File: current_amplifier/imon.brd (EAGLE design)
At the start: 76 x 16 mm, 73 parts, among them U2 OPAMP_DUALFAN4852, U4 AD8418, U5 MCP1501", U6 LTC2312-12

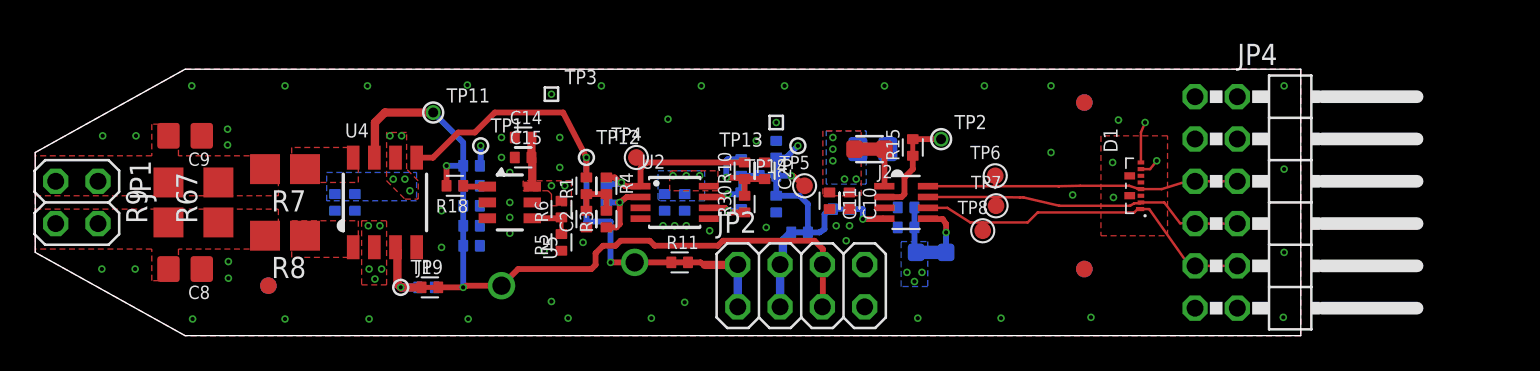
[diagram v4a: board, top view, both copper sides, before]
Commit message: imon board passes 6mil DRC.  The gain on the 4th order Bessel filter is probably wrong and needs to be redone, but the layout is ready for review
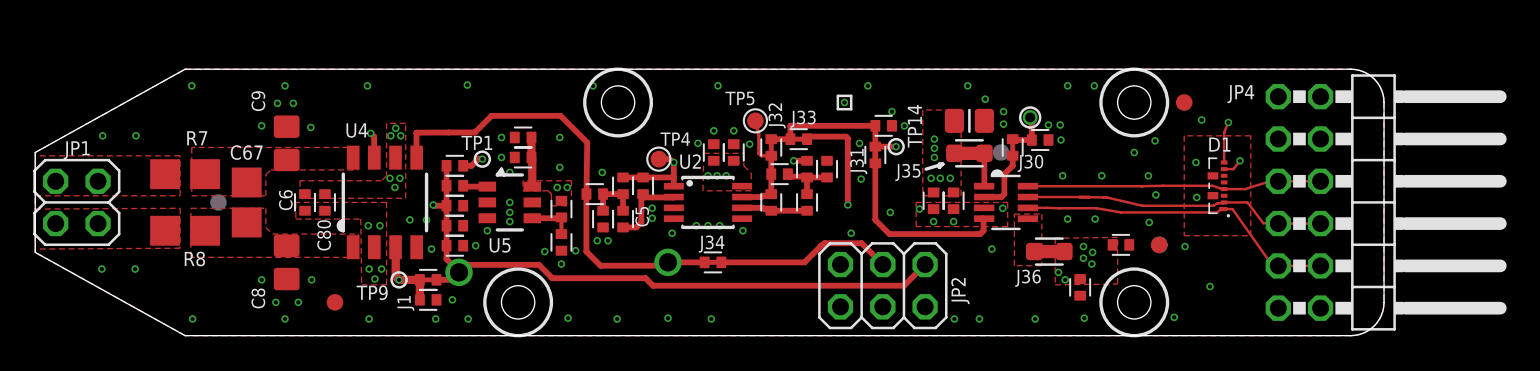
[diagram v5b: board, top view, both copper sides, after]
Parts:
- removed J2, J3: (no value), marionette:JUMPER-SHORTED-CUTTABLE-E0603-0.8MM
- removed R11, R15, R16, R17, R2: (no value), marionette:JUMPER-SHORTED-CUTTABLE-E0402-0.3MM
- removed R13, R14: np, rcl_custom:.0402-B
- removed R67, R9: np, rcl_custom:1206-0402
- removed TP11: PAD+VIA_0.6MM, marionette:PAD+VIA_0.6MM
- removed TP12: PAD+VIA_0.25MM, marionette:PAD+VIA_0.25MM
- removed TP3: PAD+VIA_GND_0.25MM, marionette:PAD+GND_VIA_0.25MM
- removed TP6, TP7, TP8: (no value), marionette:PAD-ROUND-1.0-NOCREAM+SILK
- added C16: np, rcl_custom:.0402-B
- added C67: np, rcl_custom:1206-0402
- added H1, H2, H3, H4: M2-BARE_MOUNTING_HOLE, marionette:M2-BARE_MOUNTING_HOLE
- added J30, J31, J32, J33, J34: (no value), marionette:JUMPER-SHORTED-CUTTABLE-E0402-0.3MM
- added J35, J36: (no value), marionette:JUMPER-SHORTED-CUTTABLE-E0603-0.8MM
- JP2: device pinhead:2X04 -> pinhead:2X03
- moved C12 13.1 mm to (65.2, 5.45), flipped to the top
- moved C19 11.1 mm to (62.8, 2.90), flipped to the top, turned to 270 degrees
- moved C18 6.60 mm to (51.0, 12.6), flipped to the top, turned to 180 degrees
- moved C10 6.25 mm to (55.1, 8.10)
- moved C11 6.25 mm to (54.0, 8.10)
- moved C9 6.12 mm to (15.1, 11.6), turned to 270 degrees
- moved C8 6.11 mm to (15.1, 4.40), turned to 90 degrees
- moved C13 6.04 mm to (56.1, 12.9), flipped to the top, turned to 0 degrees
- moved R7 6.01 mm to (9.00, 9.70)
- moved R8 6.01 mm to (9.00, 6.30)
- moved FIDUCIAL4 6.00 mm to (69.0, 14.0)
- moved U6 6.00 mm to (58.3, 8.00)
- moved TP14 5.90 mm to (51.7, 11.3)
- moved FIDUCIAL1 5.83 mm to (58.0, 11.0)
- moved FIDUCIAL3 5.83 mm to (11.0, 8.00)
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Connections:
- removed net V3.3D: C12.1, C19.1, D1.7, J3.2, JP4.3, JP4.4
- removed net V5D: C10.1, C11.1, C13.1, C14.2, C15.2, C3.1, C4.1, C6.1, C80.1, D1.8, J2.2, JP4.1, JP4.2, R6.2, U2.8, U4.6, U5.6
- new net VDD: C10.1, C11.1, C13.1, C14.2, C15.2, C3.1, C4.1, C6.1, C80.1, D1.8, J35.2, JP4.1, JP4.2, R6.2, U2.8, U4.6, U5.6
- new net VIO: C12.1, C19.1, D1.7, J36.2, JP4.3, JP4.4
- net ADC_AIN: now also J31.1; no longer R2.1
- net ADC_CONV: no longer TP6.PAD
- net ADC_SCK: no longer TP7.PAD
- net ADC_SDO: no longer TP8.PAD
- net ADC_VREF: now also C16.2, J30.2; no longer R15.2
- net ADC_VREF_CUTTABLE: now also J30.1; no longer R15.1
- net FILTER_2_OUT: now also J32.2; no longer R16.2
- net GND: now also C16.1, JP2.2, JP2.4, JP2.6; no longer JP2.7, JP2.8, R13.2, R14.2, TP3.TP
- net V3.3D_CUTTABLE: now also J36.1; no longer J3.1
- net V5D_CUTTABLE: now also J35.1; no longer J2.1
- net VREF_FILTERED: now also JP2.1; no longer JP2.5, JP2.6, R13.1, TP11.TP
- net VSHUNT_20X: now also J34.1; no longer R11.1, TP12.TP
- net VSHUNT_20X_OUT: now also J34.2, JP2.3; no longer JP2.1, JP2.2, R11.2
- net VSHUNT_FILTERED: now also J33.1, JP2.5; no longer JP2.3, JP2.4, R17.1
- net VSHUNT_FILTERED_ADC: now also J31.2, J32.1, J33.2; no longer R14.1, R16.1, R17.2, R2.2
- net VSHUNT_FILTERED_M: now also C67.1, C8.2
- net VSHUNT_FILTERED_P: now also C67.2, C9.2
- net VSHUNT_M: no longer C8.2, R67.1, R9.1
- net VSHUNT_P: no longer C9.2, R67.2, R9.2
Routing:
- net ADC_AIN: track 2.70 -> 12.3 mm, vias 1 -> 0
- net VDD: track 0.00 -> 5.58 mm, vias 0 -> 18
- net V5D: track 5.58 -> 0.00 mm, vias 16 -> 0
- net VSHUNT_FILTERED: track 4.85 -> 10.3 mm, vias 0 -> 1
- net VSHUNT_20X_OUT: track 6.61 -> 10.7 mm
- net V3.3D: track 3.93 -> 0.00 mm, vias 4 -> 0
- net V3.3D_CUTTABLE: track 2.96 -> 0.00 mm, vias 1 -> 0
- net FILTER_2_V1: track 6.14 -> 3.46 mm, vias 1 -> 0
- net FILTER_1_OUT: track 11.5 -> 13.6 mm, vias 1 -> 2
- net ADC_SDO: track 21.4 -> 19.5 mm
- net VSHUNT_FILTERED_ADC: track 11.3 -> 9.55 mm
- net ADC_CONV: track 19.4 -> 17.7 mm
- net VSHUNT_20X: track 25.6 -> 26.9 mm, vias 2 -> 1
- net VIO: track 0.00 -> 1.19 mm, vias 0 -> 7
- net FILTER_2_OUT: track 6.06 -> 6.95 mm, vias 2 -> 0
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- added copper zone on layer 15, net GND
- added copper zone on layer 1, net V3.3D_CUTTABLE
- added copper zone on layer 1, net VDD
- added copper zone on layer 15, net VDD
- added copper zone on layer 1, net VIO
- added copper zone on layer 15, net VIO
- removed copper zone on layer 3, net GND
- removed copper zone on layer 16, net V3.3D
- removed copper zone on layer 3, net V3.3D
- removed copper zone on layer 1, net V5D
- removed copper zone on layer 16, net V5D
- removed copper zone on layer 3, net V5D
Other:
- board size 76 x 16 mm -> 81 x 16 mm

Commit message: Changed the gain on the Bessel filter
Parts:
- C2: value 2.7n -> 750p
- C20: value 6.2n -> 1.8n
- R1: value 97.6 -> 442
- R10: value 56 -> 255
- R3: value 88.7 -> 301
- R30: value 51 -> 178
- R40: value 560 -> 562
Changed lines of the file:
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@@
 <attribute name="NAME" x="40.75" y="11" size="0.2" layer="33" ratio="15" rot="R90" align="center"/>
 </element>
-<element name="R3" library="rcl_custom" package=".0402-B" value="88.7" x="35.3" y="7" smashed="yes" rot="R90">
+<element name="R3" library="rcl_custom" package=".0402-B" value="301" x="35.3" y="7" smashed="yes" rot="R90">
 <attribute name="VALUE" x="36.9" y="6.2" size="0.8" layer="27" font="vector" ratio="15" rot="R90"/>
 <attribute name="NAME" x="35.3" y="7" size="0.2" layer="33" ratio="15" rot="R90" align="center"/>
 </element>
-<element name="R1" library="rcl_custom" package=".0402-B" value="97.6" x="33.6" y="8.5" smashed="yes" rot="R180">
+<element name="R1" library="rcl_custom" package=".0402-B" value="442" x="33.6" y="8.5" smashed="yes" rot="R180">
 <attribute name="VALUE" x="34.4" y="10.1" size="0.8" layer="27" font="vector" ratio="15" rot="R180"/>
 <attribute name="NAME" x="33.6" y="8.5" size="0.2" layer="33" ratio="15" rot="R180" align="center"/>
@@
 <attribute name="NAME" x="36.5" y="9" size="0.2" layer="33" ratio="15" rot="R90" align="center"/>
 </element>
-<element name="C2" library="rcl_custom" package=".0402-B" value="2.7n" x="34.1" y="7" smashed="yes" rot="R90">
+<element name="C2" library="rcl_custom" package=".0402-B" value="750p" x="34.1" y="7" smashed="yes" rot="R90">
 <attribute name="VALUE" x="35.7" y="6.2" size="0.8" layer="27" font="vector" ratio="15" rot="R90"/>
 <attribute name="NAME" x="34.1" y="7" size="0.2" layer="33" ratio="15" rot="R90" align="center"/>
@@
 <attribute name="NAME" x="35.3" y="9" size="0.2" layer="33" ratio="15" rot="R270" align="center"/>
 </element>
-<element name="R30" library="rcl_custom" package=".0402-B" value="51" x="46.35" y="8" smashed="yes" rot="R90">
+<element name="R30" library="rcl_custom" package=".0402-B" value="178" x="46.35" y="8" smashed="yes" rot="R90">
 <attribute name="VALUE" x="47.95" y="7.2" size="0.8" layer="27" font="vector" ratio="15" rot="R90"/>
 <attribute name="NAME" x="46.35" y="8" size="0.2" layer="33" ratio="15" rot="R90" align="center"/>
 </element>
-<element name="R10" library="rcl_custom" package=".0402-B" value="56" x="46.35" y="10" smashed="yes" rot="R90">
+<element name="R10" library="rcl_custom" package=".0402-B" value="255" x="46.35" y="10" smashed="yes" rot="R90">
 <attribute name="VALUE" x="47.95" y="9.2" size="0.8" layer="27" font="vector" ratio="15" rot="R90"/>
 <attribute name="NAME" x="46.35" y="10" size="0.2" layer="33" ratio="15" rot="R90" align="center"/>
@@
 <attribute name="NAME" x="44.2" y="8" size="0.2" layer="33" ratio="15" rot="R90" align="center"/>
 </element>
-<element name="C20" library="rcl_custom" package=".0402-B" value="6.2n" x="47.55" y="10" smashed="yes" rot="R270">
+<element name="C20" library="rcl_custom" package=".0402-B" value="1.8n" x="47.55" y="10" smashed="yes" rot="R270">
 <attribute name="VALUE" x="45.95" y="10.8" size="0.8" layer="27" font="vector" ratio="15" rot="R270"/>
 <attribute name="NAME" x="47.55" y="10" size="0.2" layer="33" ratio="15" rot="R270" align="center"/>
 </element>
-<element name="R40" library="rcl_custom" package=".0402-B" value="560" x="44.7" y="9.7" smashed="yes">
+<element name="R40" library="rcl_custom" package=".0402-B" value="562" x="44.7" y="9.7" smashed="yes">
 <attribute name="VALUE" x="43.9" y="8.1" size="0.8" layer="27" font="vector" ratio="15"/>
 <attribute name="NAME" x="44.7" y="9.7" size="0.2" layer="33" ratio="15" align="center"/>

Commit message: Gerber files and small layout changes to the imon.brd
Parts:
- added R2: 10k, rcl_custom:.0402-B
- moved H2 6.00 mm to (29.0, 14.0)
- moved C14 2.25 mm to (31.2, 10.7), turned to 180 degrees
- moved J34 1.38 mm to (39.6, 5.30)
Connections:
- net ADC_CONV: now also R2.2
- net VIO: now also R2.1
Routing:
- net ADC_CONV: track 17.7 -> 25.7 mm
- net VSHUNT_20X: track 26.9 -> 23.4 mm
- net VSHUNT_20X_OUT: track 10.7 -> 11.4 mm
- added copper zone on layer 3, net GND
- added copper zone on layer 3, net VDD
- added copper zone on layer 3, net VIO
- removed copper zone on layer 15, net GND
- removed copper zone on layer 15, net VDD
- removed copper zone on layer 15, net VIO
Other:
- board text added: "M"
- board text added: "P"
- board text added: "VREF_FIL"
- board text added: "VSHNT_20X"
- board text added: "VSHNT_F"
